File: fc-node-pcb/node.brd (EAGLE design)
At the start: 50 x 24 mm, 15 parts, among them J1 AVR_SPI_PRG_62X3_LOCK

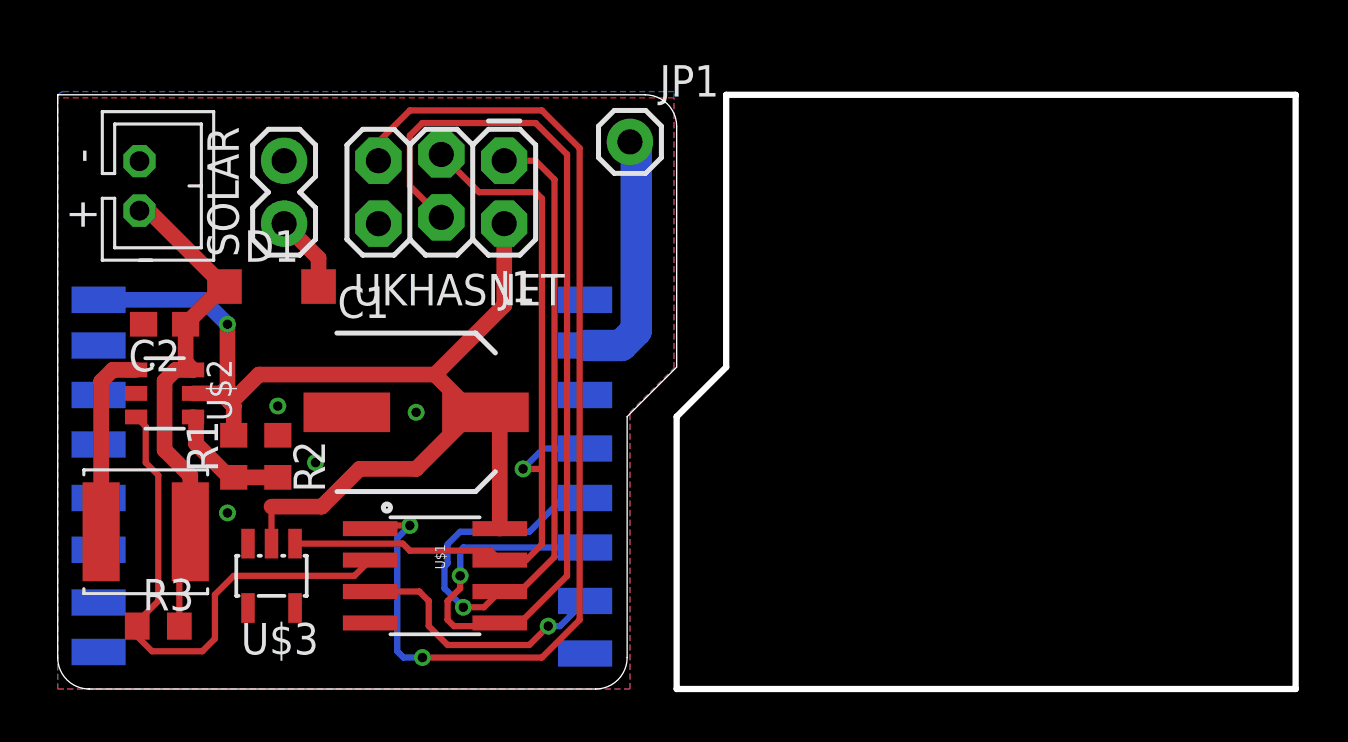
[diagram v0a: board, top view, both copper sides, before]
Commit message: finished routing fc node
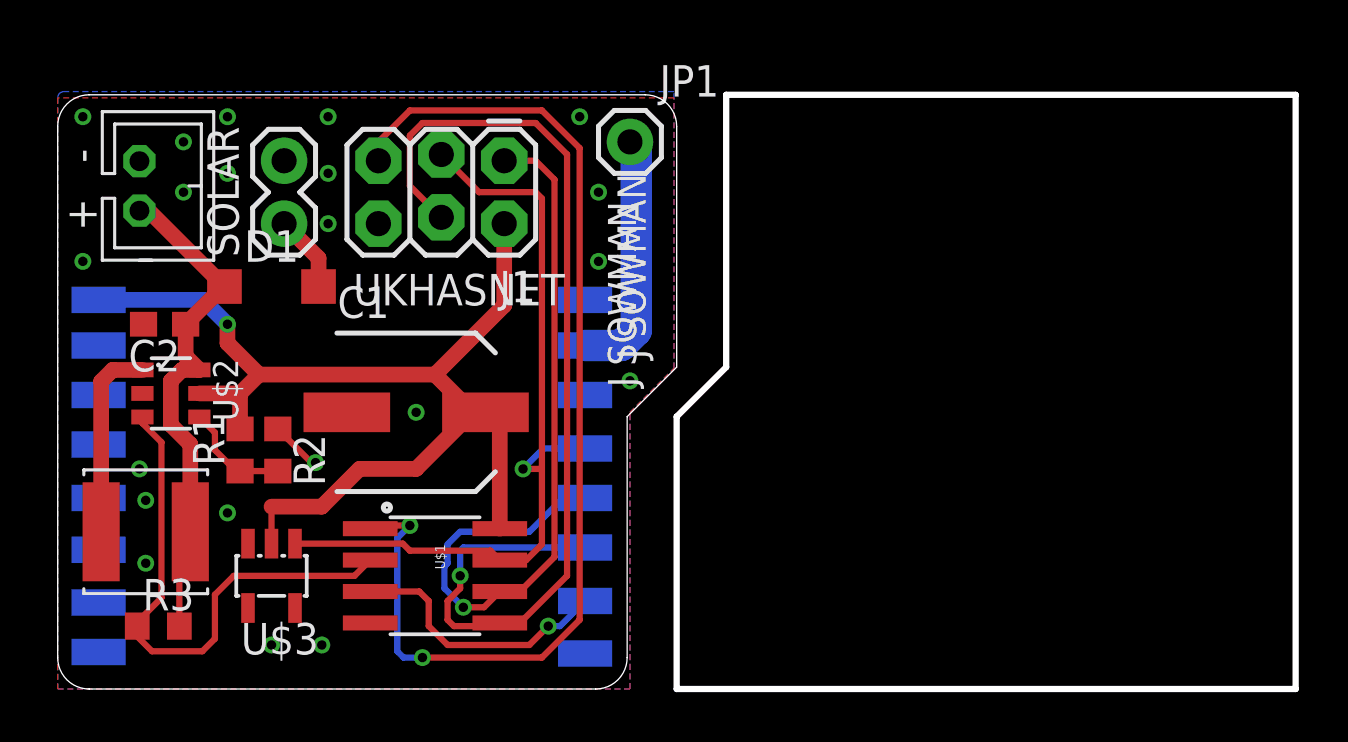
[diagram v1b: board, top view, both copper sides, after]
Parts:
- moved R1 0.36 mm to (7.37, 9.65)
- moved U$2 0.25 mm to (4.57, 11.9)
- moved R2 0.25 mm to (8.89, 9.65)
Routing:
- net GND: track 0.00 -> 2.09 mm, vias 4 -> 21
- net VCC: track 46.3 -> 45.5 mm
- net N$2: track 5.00 -> 4.49 mm
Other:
- outline, holes or cut-outs redrawn
- board text added: "+"
- board text added: "J SOWMAN"
- board text added: "MAR '15"
